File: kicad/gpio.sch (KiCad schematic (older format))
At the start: 7 parts, among them U1_301 TMS320F28388DZWTS

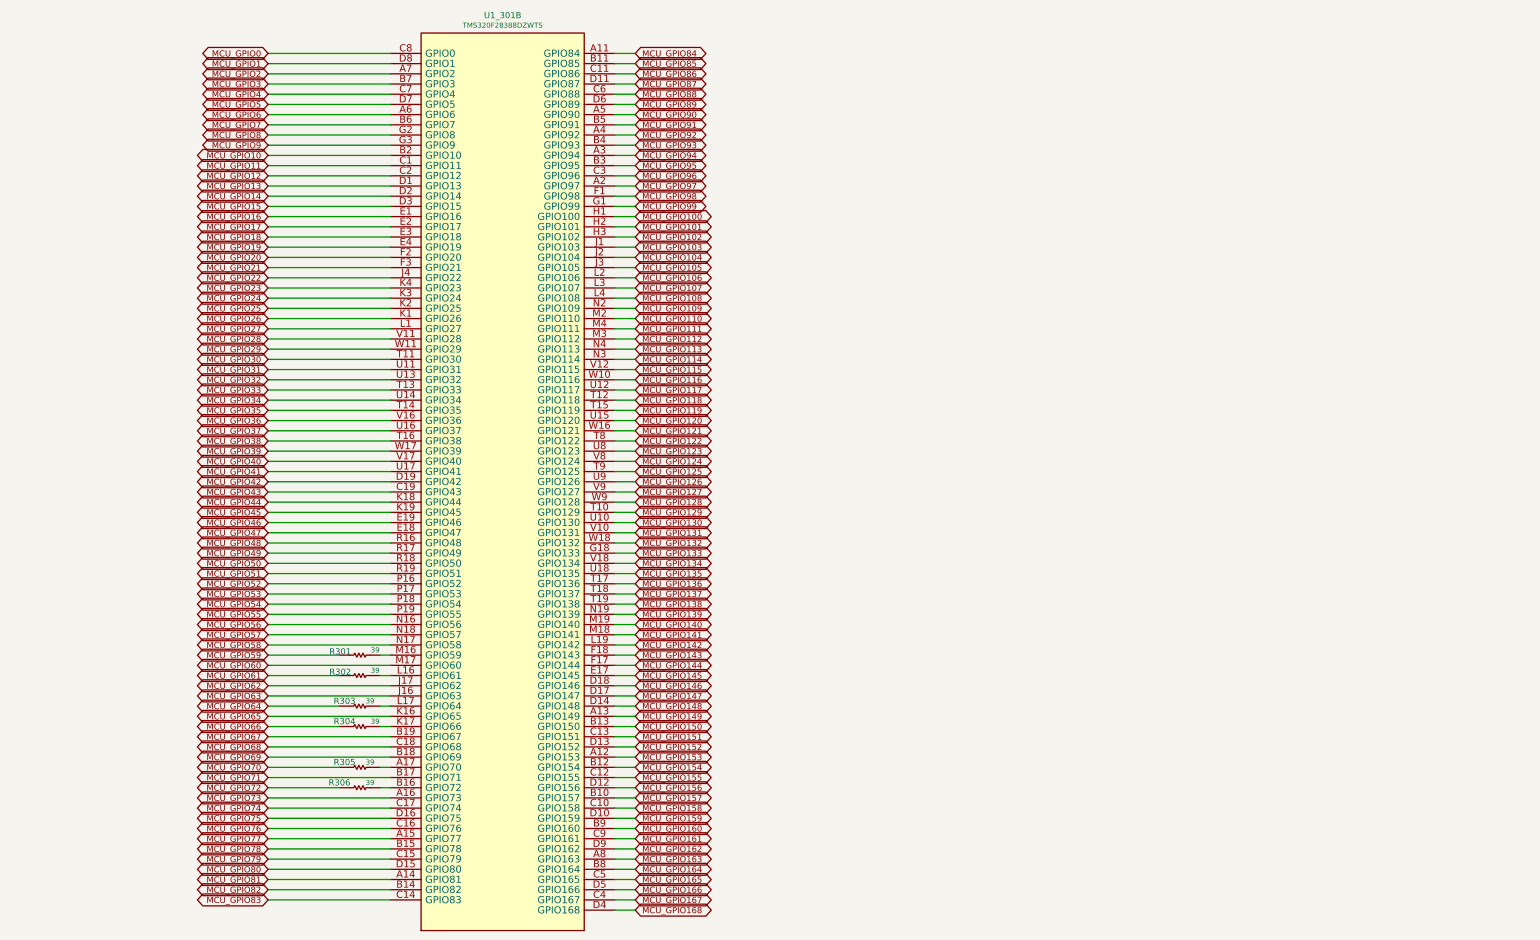
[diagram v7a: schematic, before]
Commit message: I've connected interfaces to gpio and change some muxes
I've changed some muxes reading the datasheet to group same kind of
signals, now it's time to add encoders input
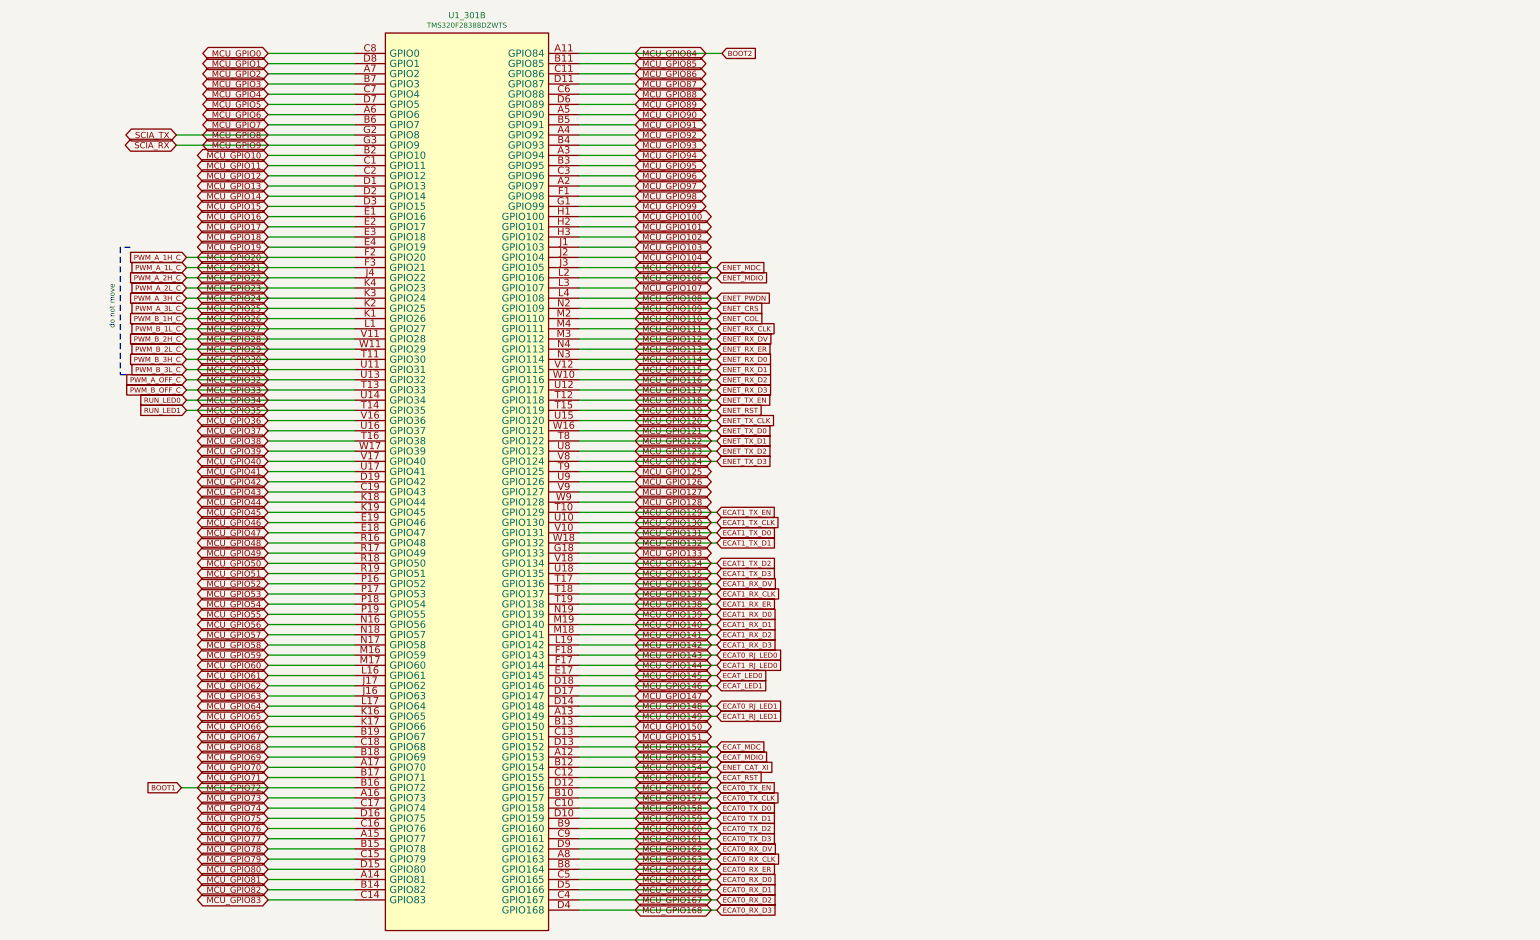
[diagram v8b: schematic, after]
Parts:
- removed R301, R302, R303, R304, R305, R306: 39, symbol servo:Resistor
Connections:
- net MCU_GPIO59: now also U1_301.M16 (GPIO59)
- net MCU_GPIO61: now also U1_301.L16 (GPIO61)
- net MCU_GPIO64: now also U1_301.L17 (GPIO64)
- net MCU_GPIO66: now also U1_301.K17 (GPIO66)
- net MCU_GPIO70: now also U1_301.A17 (GPIO70)
- net BOOT1: now reaches U1_301.B16 (GPIO72)
- net MCU_GPIO105 renamed ENET_MDC
- net MCU_GPIO106 renamed ENET_MDIO
- net MCU_GPIO108 renamed ENET_PWDN
- net MCU_GPIO109 renamed ENET_CRS
- net MCU_GPIO110 renamed ENET_COL
- net MCU_GPIO111 renamed ENET_RX_CLK
- net MCU_GPIO112 renamed ENET_RX_DV
- net MCU_GPIO113 renamed ENET_RX_ER
- net MCU_GPIO114 renamed ENET_RX_D0
- net MCU_GPIO115 renamed ENET_RX_D1
- net MCU_GPIO116 renamed ENET_RX_D2
- net MCU_GPIO117 renamed ENET_RX_D3
- net MCU_GPIO118 renamed ENET_TX_EN
- net MCU_GPIO119 renamed ENET_RST
- net MCU_GPIO120 renamed ENET_TX_CLK
- net MCU_GPIO121 renamed ENET_TX_D0
- net MCU_GPIO122 renamed ENET_TX_D1
- net MCU_GPIO123 renamed ENET_TX_D2
- net MCU_GPIO124 renamed ENET_TX_D3
- net MCU_GPIO129 renamed ECAT1_TX_EN
- net MCU_GPIO130 renamed ECAT1_TX_CLK
- net MCU_GPIO131 renamed ECAT1_TX_D0
- net MCU_GPIO132 renamed ECAT1_TX_D1
- net MCU_GPIO134 renamed ECAT1_TX_D2
- net MCU_GPIO135 renamed ECAT1_TX_D3
- net MCU_GPIO136 renamed ECAT1_RX_DV
- net MCU_GPIO137 renamed ECAT1_RX_CLK
- net MCU_GPIO138 renamed ECAT1_RX_ER
- net MCU_GPIO139 renamed ECAT1_RX_D0
- net MCU_GPIO140 renamed ECAT1_RX_D1
- net MCU_GPIO141 renamed ECAT1_RX_D2
- net MCU_GPIO142 renamed ECAT1_RX_D3
- net MCU_GPIO143 renamed ECAT0_RJ_LED0
- net MCU_GPIO144 renamed ECAT1_RJ_LED0
- net MCU_GPIO145 renamed ECAT_LED0
- net MCU_GPIO146 renamed ECAT_LED1
- net MCU_GPIO148 renamed ECAT0_RJ_LED1
- net MCU_GPIO149 renamed ECAT1_RJ_LED1
- net MCU_GPIO152 renamed ECAT_MDC
- net MCU_GPIO153 renamed ECAT_MDIO
- net MCU_GPIO154 renamed ENET_CAT_XI
- net MCU_GPIO155 renamed ECAT_RST
- net MCU_GPIO156 renamed ECAT0_TX_EN
- net MCU_GPIO157 renamed ECAT0_TX_CLK
- net MCU_GPIO158 renamed ECAT0_TX_D0
- net MCU_GPIO159 renamed ECAT0_TX_D1
- net MCU_GPIO160 renamed ECAT0_TX_D2
- net MCU_GPIO161 renamed ECAT0_TX_D3
- net MCU_GPIO162 renamed ECAT0_RX_DV
- net MCU_GPIO163 renamed ECAT0_RX_CLK
- net MCU_GPIO164 renamed ECAT0_RX_ER
- net MCU_GPIO165 renamed ECAT0_RX_D0
- net MCU_GPIO166 renamed ECAT0_RX_D1
- net MCU_GPIO167 renamed ECAT0_RX_D2
- net MCU_GPIO168 renamed ECAT0_RX_D3
- net MCU_GPIO84 renamed BOOT2
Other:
- note added: "do not move"
- moved on the sheet: U1_301B
